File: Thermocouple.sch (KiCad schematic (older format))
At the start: 1 part, among them U5 MAX31855KASA+

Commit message: more components added
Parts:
- added C12, C9: 0.1uF, Capacitors_SMD:c_1206, symbol C
- added U5: 74LVC2G34, SMD_Packages:SOT-23-6, symbol 74LVC2G34
- added U?: 74LVC1T45, symbol 74LVC1T45
- renumbered U5 to U7
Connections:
- net GND: now reaches U7.1 (GND)
- net GND: now also C12.2, C9.2, U5.2 (GND), U5.2 (GND)
- net +3.3V: now reaches U7.4 (Vcc)
- net +3.3V: now also C12.1, C9.1
- net at U7.5 (SCK): now also U5.6
- net at U7.6 (~CS): now also U5.4
- new net VCC: U5.5 (VCC), U5.5 (VCC)
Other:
- moved on the sheet: U7
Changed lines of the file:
@@
 LIBS:atmel
 LIBS:power
+LIBS:74xgxx
+LIBS:74xx
 LIBS:ReflowToaster-cache
 EELAYER 24 0
@@
 $EndDescr
 $Comp
-L MAX31855KASA+ U5
+L MAX31855KASA+ U7
 U 1 1 540FF176
-P 4800 3150
-F 0 "U5" H 4575 3425 60  0000 L CNN
-F 1 "MAX31855KASA+" H 4800 2875 60  0000 C CNN
-F 2 "SMD_Packages:SOIC-8-N" H 4800 4025 60  0001 C CNN
-F 3 "http://datasheets.maxim-ic.com/en/ds/MAX31855.pdf" H 4800 4100 60  0001 C CNN
-F 4 "Maxim" H 4800 4175 60  0001 C CNN "Manufacturer"
-F 5 "MAX31855KASA+" H 4800 4250 60  0001 C CNN "Part Number"
-	1    4800 3150
+P 4750 3150
+F 0 "U7" H 4525 3425 60  0000 L CNN
+F 1 "MAX31855KASA+" H 4750 2875 60  0000 C CNN
+F 2 "SMD_Packages:SOIC-8-N" H 4750 4025 60  0001 C CNN
+F 3 "http://datasheets.maxim-ic.com/en/ds/MAX31855.pdf" H 4750 4100 60  0001 C CNN
+F 4 "Maxim" H 4750 4175 60  0001 C CNN "Manufacturer"
+F 5 "MAX31855KASA+" H 4750 4250 60  0001 C CNN "Part Number"
+	1    4750 3150
 	1    0    0    -1
 $EndComp
+$Comp
+L 74LVC2G34 U5
+U 1 1 5410697C
+P 3850 2750
+F 0 "U5" H 3750 2900 40  0000 C CNN
+F 1 "74LVC2G34" H 3850 2600 40  0000 C CNN
+F 2 "SMD_Packages:SOT-23-6" H 3850 2750 60  0001 C CNN
+F 3 "http://datasheet.octopart.com/SN74LVC2G34DBVR-Texas-Instruments-datasheet-153323.pdf" H 3850 2750 60  0001 C CNN
+F 4 "Texas Instruments" H 3850 2750 60  0001 C CNN "Manufacturer"
+F 5 "SN74LVC2G34DBVR" H 3850 2750 60  0001 C CNN "Part Number"
+	1    3850 2750
+	1    0    0    -1
+$EndComp
+$Comp
+L 74LVC2G34 U5
+U 2 1 54106A65
+P 3850 3100
+F 0 "U5" H 3750 3250 40  0000 C CNN
+F 1 "74LVC2G34" H 3850 2950 40  0000 C CNN
+F 2 "" H 3850 3100 60  0000 C CNN
+F 3 "" H 3850 3100 60  0000 C CNN
+	2    3850 3100
+	1    0    0    -1
+$EndComp
+Wire Wire Line
+	4100 3100 4350 3100
+Wire Wire Line
+	4350 3000 4200 3000
+Wire Wire Line
+	4200 3000 4200 2750
+Wire Wire Line
+	4200 2750 4100 2750
+$Comp
+L C C9
+U 1 1 54106B7B
+P 3900 2200
+F 0 "C9" H 3900 2300 40  0000 L CNN
+F 1 "0.1uF" H 3906 2115 40  0000 L CNN
+F 2 "Capacitors_SMD:c_1206" H 3938 2050 30  0001 C CNN
+F 3 "" H 3900 2200 60  0000 C CNN
+F 4 "U5 Bypass" H 4100 2050 40  0000 C CNN "Usage"
+	1    3900 2200
+	1    0    0    -1
+$EndComp
+$Comp
+L +3.3V #PWR?
+U 1 1 54106BA8
+P 3900 1950
+F 0 "#PWR?" H 3900 1910 30  0001 C CNN
+F 1 "+3.3V" H 3900 2060 30  0000 C CNN
+F 2 "" H 3900 1950 60  0000 C CNN
+F 3 "" H 3900 1950 60  0000 C CNN
+	1    3900 1950
+	1    0    0    -1
+$EndComp
+$Comp
+L GND #PWR?
+U 1 1 54106BBC
+P 3900 2450
+F 0 "#PWR?" H 3900 2450 30  0001 C CNN
+F 1 "GND" H 3900 2380 30  0001 C CNN
+F 2 "" H 3900 2450 60  0000 C CNN
+F 3 "" H 3900 2450 60  0000 C CNN
+	1    3900 2450
+	1    0    0    -1
+$EndComp
+Wire Wire Line
+	3900 2450 3900 2400
+Wire Wire Line
+	3900 1950 3900 2000
+$Comp
+L C C12
+U 1 1 54106D7A
+P 4950 2600
+F 0 "C12" V 4900 2400 40  0000 L CNN
+F 1 "0.1uF" V 5000 2650 40  0000 L CNN
+F 2 "Capacitors_SMD:c_1206" H 4988 2450 30  0001 C CNN
+F 3 "" H 4950 2600 60  0000 C CNN
+	1    4950 2600
+	0    1    1    0
+$EndComp
+$Comp
+L +3.3V #PWR?
+U 1 1 54106ED2
+P 5200 2550
+F 0 "#PWR?" H 5200 2510 30  0001 C CNN
+F 1 "+3.3V" H 5200 2660 30  0000 C CNN
+F 2 "" H 5200 2550 60  0000 C CNN
+F 3 "" H 5200 2550 60  0000 C CNN
+	1    5200 2550
+	1    0    0    -1
+$EndComp
+$Comp
+L GND #PWR?
+U 1 1 54106EE6
+P 4700 2650
+F 0 "#PWR?" H 4700 2650 30  0001 C CNN
+F 1 "GND" H 4700 2580 30  0001 C CNN
+F 2 "" H 4700 2650 60  0000 C CNN
+F 3 "" H 4700 2650 60  0000 C CNN
+	1    4700 2650
+	1    0    0    -1
+$EndComp
+Wire Wire Line
+	4700 2650 4700 2600
+Wire Wire Line
+	4700 2600 4750 2600
+Wire Wire Line
+	5200 2550 5200 3000
+Wire Wire Line
+	5200 2600 5150 2600
+Wire Wire Line
+	5200 3000 5150 3000
+Connection ~ 5200 2600
+$Comp
+L GND #PWR?
+U 1 1 54106BFC
+P 5200 3350
+F 0 "#PWR?" H 5200 3350 30  0001 C CNN
+F 1 "GND" H 5200 3280 30  0001 C CNN
+F 2 "" H 5200 3350 60  0000 C CNN
+F 3 "" H 5200 3350 60  0000 C CNN
+	1    5200 3350
+	1    0    0    -1
+$EndComp
+Wire Wire Line
+	5150 3300 5200 3300
+Wire Wire Line
+	5200 3300 5200 3350
+$Comp
+L 74LVC1T45 U?
+U 1 1 54106E70
+P 3450 3850
+F 0 "U?" H 3325 4150 60  0000 R CNN
+F 1 "74LVC1T45" H 3475 3550 60  0000 L CNN
+F 2 "" H 3450 3850 60  0000 C CNN
+F 3 "http://datasheet.octopart.com/SN74LVC1T45DBVR-Texas-Instruments-datasheet-21259457.pdf" H 3450 4725 60  0001 C CNN
+	1    3450 3850
+	1    0    0    -1
+$EndComp

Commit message: working on thermocouple section now
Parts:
- added C10, C11: 0.1uF, Capacitors_SMD:c_1206, symbol C
- added C13: 0.01uF, Capacitors_SMD:c_1206, symbol C
- U6: renamed from U?; footprint (none) -> SMD_Packages:SOT-23-6; Manufacturer (none) -> Texas Instruments; Part Number (none) -> SN74LVC1T45DBVR
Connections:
- net +3.3V: now also U6.6 (VccB), C11.1
- net GND: now also U6.2 (GND), U6.5 (DIR), C10.2, C11.2
- net at U7.2 (T-): now also C13.2
- net at U7.3 (T+): now also C13.1
- net at U7.7 (SO): now also U6.4 (B)
- net A1: now reaches U5.1
- net A2: now reaches U5.3
- net +5V: now reaches U6.1 (VccA)
- net +5V: now also C10.1
- net A3: now reaches U6.3 (A)
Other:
- moved on the sheet: C9, U6
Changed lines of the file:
@@
 L C C9
 U 1 1 54106B7B
-P 3900 2200
-F 0 "C9" H 3900 2300 40  0000 L CNN
-F 1 "0.1uF" H 3906 2115 40  0000 L CNN
-F 2 "Capacitors_SMD:c_1206" H 3938 2050 30  0001 C CNN
-F 3 "" H 3900 2200 60  0000 C CNN
-F 4 "U5 Bypass" H 4100 2050 40  0000 C CNN "Usage"
-	1    3900 2200
+P 3850 3750
+F 0 "C9" H 3850 3850 40  0000 L CNN
+F 1 "0.1uF" H 3856 3665 40  0000 L CNN
+F 2 "Capacitors_SMD:c_1206" H 3888 3600 30  0001 C CNN
+F 3 "" H 3850 3750 60  0000 C CNN
+F 4 "U5 Bypass" H 4050 3600 40  0000 C CNN "Usage"
+	1    3850 3750
 	1    0    0    -1
 $EndComp
@@
 L +3.3V #PWR?
 U 1 1 54106BA8
-P 3900 1950
-F 0 "#PWR?" H 3900 1910 30  0001 C CNN
-F 1 "+3.3V" H 3900 2060 30  0000 C CNN
-F 2 "" H 3900 1950 60  0000 C CNN
-F 3 "" H 3900 1950 60  0000 C CNN
-	1    3900 1950
+P 3850 3500
+F 0 "#PWR?" H 3850 3460 30  0001 C CNN
+F 1 "+3.3V" H 3850 3610 30  0000 C CNN
+F 2 "" H 3850 3500 60  0000 C CNN
+F 3 "" H 3850 3500 60  0000 C CNN
+	1    3850 3500
 	1    0    0    -1
 $EndComp
@@
 L GND #PWR?
 U 1 1 54106BBC
-P 3900 2450
-F 0 "#PWR?" H 3900 2450 30  0001 C CNN
-F 1 "GND" H 3900 2380 30  0001 C CNN
-F 2 "" H 3900 2450 60  0000 C CNN
-F 3 "" H 3900 2450 60  0000 C CNN
-	1    3900 2450
-	1    0    0    -1
-$EndComp
-Wire Wire Line
-	3900 2450 3900 2400
-Wire Wire Line
-	3900 1950 3900 2000
+P 3850 4000
+F 0 "#PWR?" H 3850 4000 30  0001 C CNN
+F 1 "GND" H 3850 3930 30  0001 C CNN
+F 2 "" H 3850 4000 60  0000 C CNN
+F 3 "" H 3850 4000 60  0000 C CNN
+	1    3850 4000
+	1    0    0    -1
+$EndComp
+Wire Wire Line
+	3850 4000 3850 3950
+Wire Wire Line
+	3850 3500 3850 3550
 $Comp
 L C C12
@@
 	5200 3300 5200 3350
 $Comp
-L 74LVC1T45 U?
+L 74LVC1T45 U6
 U 1 1 54106E70
-P 3450 3850
-F 0 "U?" H 3325 4150 60  0000 R CNN
-F 1 "74LVC1T45" H 3475 3550 60  0000 L CNN
-F 2 "" H 3450 3850 60  0000 C CNN
-F 3 "http://datasheet.octopart.com/SN74LVC1T45DBVR-Texas-Instruments-datasheet-21259457.pdf" H 3450 4725 60  0001 C CNN
-	1    3450 3850
-	1    0    0    -1
-$EndComp
+P 2950 4150
+F 0 "U6" H 2825 4450 60  0000 R CNN
+F 1 "74LVC1T45" H 2975 3850 60  0000 L CNN
+F 2 "SMD_Packages:SOT-23-6" H 2950 4150 60  0001 C CNN
+F 3 "http://datasheet.octopart.com/SN74LVC1T45DBVR-Texas-Instruments-datasheet-21259457.pdf" H 2950 5025 60  0001 C CNN
+F 4 "Texas Instruments" H 2950 4150 60  0001 C CNN "Manufacturer"
+F 5 "SN74LVC1T45DBVR" H 2950 4150 60  0001 C CNN "Part Number"
+	1    2950 4150
+	1    0    0    -1
+$EndComp
+Wire Wire Line
+	4350 3200 4200 3200
+Wire Wire Line
+	4200 3200 4200 4150
+Wire Wire Line
+	4200 4150 3300 4150
+$Comp
+L C C10
+U 1 1 541074BF
+P 2750 3450
+F 0 "C10" H 2750 3550 40  0000 L CNN
+F 1 "0.1uF" H 2756 3365 40  0000 L CNN
+F 2 "Capacitors_SMD:c_1206" H 2788 3300 30  0001 C CNN
+F 3 "" H 2750 3450 60  0000 C CNN
+	1    2750 3450
+	1    0    0    -1
+$EndComp
+$Comp
+L C C11
+U 1 1 54107549
+P 3150 3450
+F 0 "C11" H 3150 3550 40  0000 L CNN
+F 1 "0.1uF" H 3156 3365 40  0000 L CNN
+F 2 "Capacitors_SMD:c_1206" H 3188 3300 30  0001 C CNN
+F 3 "" H 3150 3450 60  0000 C CNN
+	1    3150 3450
+	1    0    0    -1
+$EndComp
+$Comp
+L +3.3V #PWR?
+U 1 1 54107680
+P 3150 3200
+F 0 "#PWR?" H 3150 3160 30  0001 C CNN
+F 1 "+3.3V" H 3150 3310 30  0000 C CNN
+F 2 "" H 3150 3200 60  0000 C CNN
+F 3 "" H 3150 3200 60  0000 C CNN
+	1    3150 3200
+	1    0    0    -1
+$EndComp
+$Comp
+L +5V #PWR?
+U 1 1 5410769C
+P 2750 3200
+F 0 "#PWR?" H 2750 3290 20  0001 C CNN
+F 1 "+5V" H 2750 3290 30  0000 C CNN
+F 2 "" H 2750 3200 60  0000 C CNN
+F 3 "" H 2750 3200 60  0000 C CNN
+	1    2750 3200
+	1    0    0    -1
+$EndComp
+$Comp
+L GND #PWR?
+U 1 1 541076B0
+P 3150 3700
+F 0 "#PWR?" H 3150 3700 30  0001 C CNN
+F 1 "GND" H 3150 3630 30  0001 C CNN
+F 2 "" H 3150 3700 60  0000 C CNN
+F 3 "" H 3150 3700 60  0000 C CNN
+	1    3150 3700
+	1    0    0    -1
+$EndComp
+$Comp
+L GND #PWR?
+U 1 1 541076C4
+P 2750 3700
+F 0 "#PWR?" H 2750 3700 30  0001 C CNN
+F 1 "GND" H 2750 3630 30  0001 C CNN
+F 2 "" H 2750 3700 60  0000 C CNN
+F 3 "" H 2750 3700 60  0000 C CNN
+	1    2750 3700
+	1    0    0    -1
+$EndComp
+Wire Wire Line
+	2750 3700 2750 3650
+Wire Wire Line
+	3150 3650 3150 3700
+Wire Wire Line
+	2750 3200 2750 3250
+Wire Wire Line
+	2750 3250 2900 3250
+Wire Wire Line
+	2900 3250 2900 3800
+Wire Wire Line
+	3000 3800 3000 3250
+Wire Wire Line
+	3000 3250 3150 3250
+Wire Wire Line
+	3150 3250 3150 3200
+$Comp
+L GND #PWR?
+U 1 1 54107794
+P 2950 4550
+F 0 "#PWR?" H 2950 4550 30  0001 C CNN
+F 1 "GND" H 2950 4480 30  0001 C CNN
+F 2 "" H 2950 4550 60  0000 C CNN
+F 3 "" H 2950 4550 60  0000 C CNN
+	1    2950 4550
+	1    0    0    -1
+$EndComp
+$Comp
+L GND #PWR?
+U 1 1 541077B0
+P 2550 4300
+F 0 "#PWR?" H 2550 4300 30  0001 C CNN
+F 1 "GND" H 2550 4230 30  0001 C CNN
+F 2 "" H 2550 4300 60  0000 C CNN
+F 3 "" H 2550 4300 60  0000 C CNN
+	1    2550 4300
+	1    0    0    -1
+$EndComp
+Wire Wire Line
+	2550 4300 2550 4250
+Wire Wire Line
+	2550 4250 2600 4250
+Wire Wire Line
+	2950 4500 2950 4550
+Text HLabel 2400 4150 0    60   Output ~ 0
+A3
+Wire Wire Line
+	2400 4150 2600 4150
+Text HLabel 2400 2750 0    60   Input ~ 0
+A1
+Text HLabel 2400 2850 0    60   Input ~ 0
+A2
+Wire Wire Line
+	2400 2750 3550 2750
+Wire Wire Line
+	3550 3100 3550 2850
+Wire Wire Line
+	3550 2850 2400 2850
+$Comp
+L C C13
+U 1 1 54107DF0
+P 5650 3150
+F 0 "C13" H 5650 3250 40  0000 L CNN
+F 1 "0.01uF" H 5656 3065 40  0000 L CNN
+F 2 "Capacitors_SMD:c_1206" H 5688 3000 30  0001 C CNN
+F 3 "" H 5650 3150 60  0000 C CNN
+	1    5650 3150
+	1    0    0    -1
+$EndComp
+Wire Wire Line
+	5150 3100 5400 3100
+Wire Wire Line
+	5400 3100 5400 2950
+Wire Wire Line
+	5400 2950 5650 2950
+Wire Wire Line
+	5150 3200 5400 3200
+Wire Wire Line
+	5400 3200 5400 3350
+Wire Wire Line
+	5400 3350 5650 3350
 $EndSCHEMATC

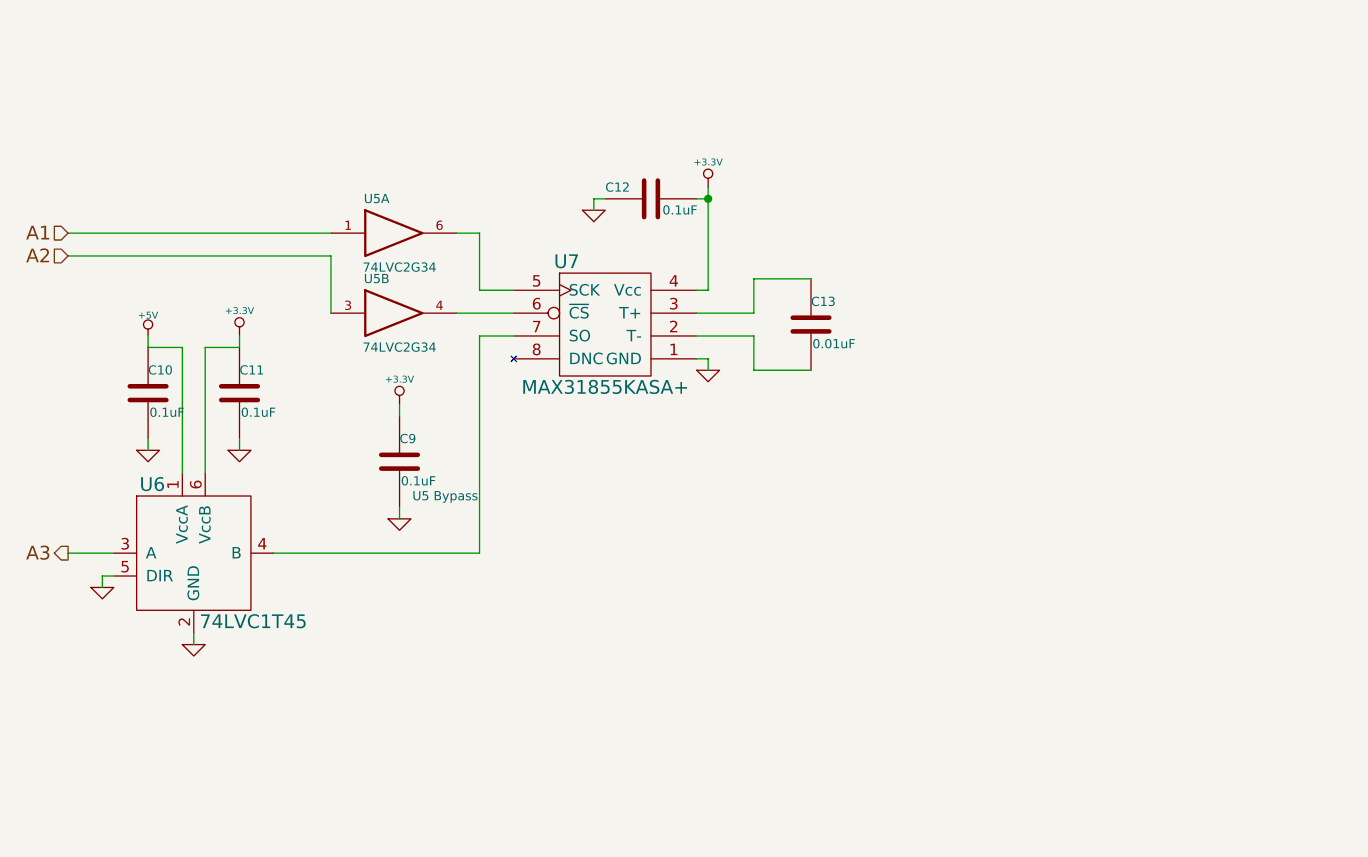
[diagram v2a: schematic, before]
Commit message: thermocouple section complete
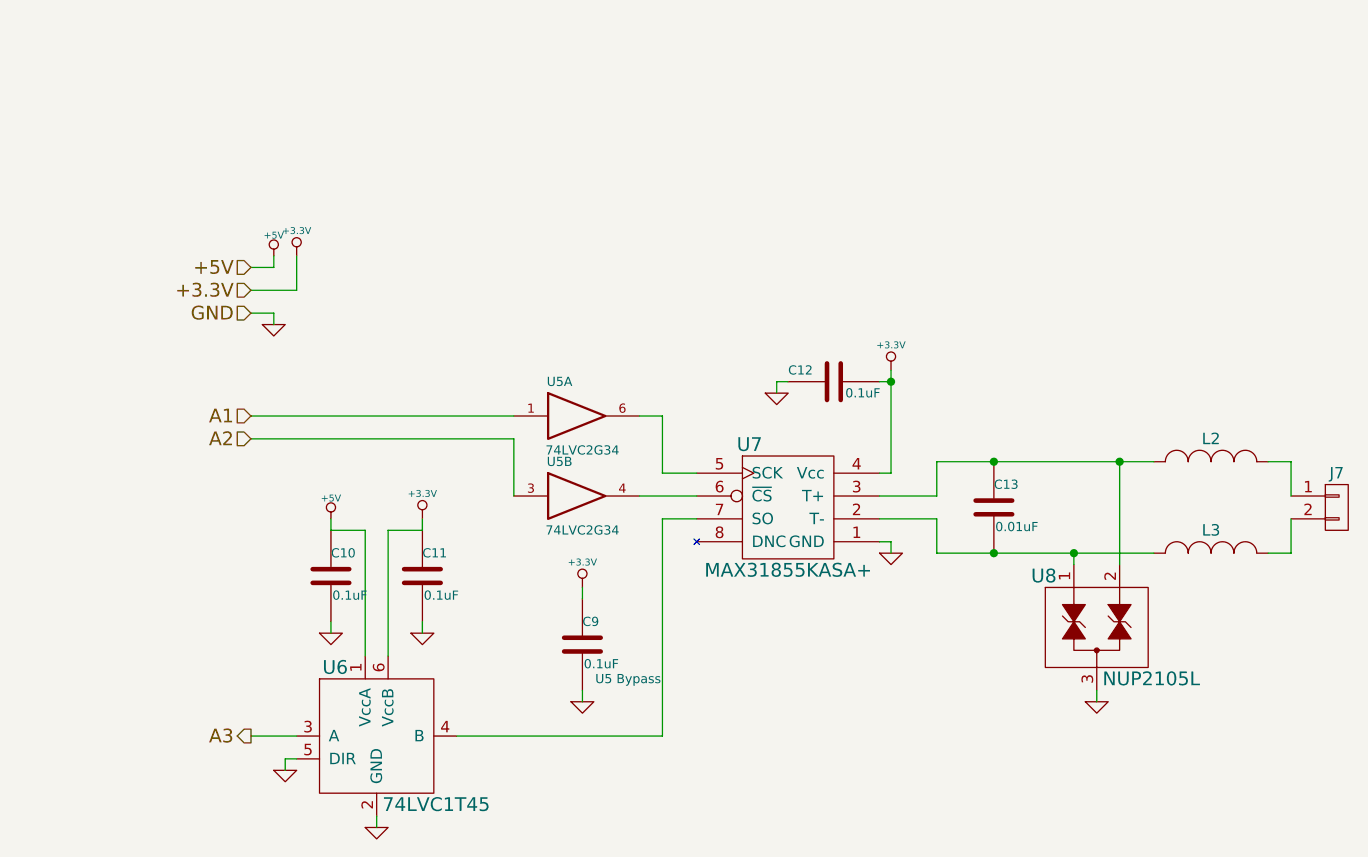
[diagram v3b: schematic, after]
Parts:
- added J7: CONN_01X02, ReflowToaster:282836-2, symbol CONN_01X02
- added L2, L3: INDUCTOR_SMALL, ReflowToaster:smd_1806, symbol INDUCTOR_SMALL
- added U8: NUP2105L, SMD_Packages:SOT-23, symbol NUP2105L
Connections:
- net GND: now also U8.3
- net at C13.2, U7.2 (T-): now also L3.1, U8.1
- net at C13.1, U7.3 (T+): now also L2.1, U8.2
- new net: J7.1 (P1), L2.2
- new net: J7.2 (P2), L3.2
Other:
- moved on the sheet: C10, C11, C12, C13, C9, U5A, U5B, U6, U7
